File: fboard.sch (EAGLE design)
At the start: 41 parts, among them U1 ATMEGA328PB-AU, U2 MPU-6050

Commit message: fixed schematic
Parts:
- removed C8: 0.1uF, rcl:C-USC0805
- removed R12: 330R, rcl:R-US_R0805
- removed R13: 2.7kR, rcl:R-US_R0805
- removed R14, R15: 4.7kR, rcl:R-US_R0805
- removed U$1: SS14, SS14:SS14
- removed U$2: SK-3296S-01-L1, CustomParts:SK-3296S-01-L1
- removed U$3: RK-2032, CustomParts:RK-2032
- added BAT1: RK-2032, CustomParts:RK-2032
- added D1: MBR0520LT, diode:MBR0520LT
- added Q1: SL2305, SL2305:SL2305
- added S1: SK-3296S-01-L1, CustomParts:SK-3296S-01-L1
- added U3: SN74HC138PW, SN74HC138PW:SN74HC138PW
- C1, C2, C3, C4: device rcl:C-USC0805 -> rcl:C-EUC0805
- C5: value 0.1uF -> 10nF; device rcl:C-USC0805 -> rcl:C-EUC0805
- C6: value 10nF -> 2nF; device rcl:C-USC0805 -> rcl:C-EUC0805
- C7: value 2nF -> 0.1uF; device rcl:C-USC0805 -> rcl:C-EUC0805
- R1, R2, R3, R4, R5, R6, R7, R8, R9: device rcl:R-US_R0805 -> rcl:R-EU_R0805
- R10, R11: value 330R -> 4.7kR; device rcl:R-US_R0805 -> rcl:R-EU_R0805
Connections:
- removed net B3: ISP1.MOSI, R10.1
- removed net B4: ISP1.MISO, R11.2
- removed net B5: ISP1.SCK, R12.2
- removed net N$10: LED4.A, R4.2
- removed net N$11: LED9.A, R5.2
- removed net N$12: LED5.A, R6.2
- removed net N$13: LED6.A, R7.2
- removed net N$14: LED7.A, R8.2
- removed net N$15: LED8.A, R9.2
- removed net N$16: U$1.C, U$2.3
- removed net N$2: LED1.A, R1.2
- removed net PB0: R6.1, U1.PB0(ICP1/CLKO/PTCXY)
- removed net PB1: R5.1, U1.PB1(OC1A/PTCXY)
- removed net PB2: R4.1, U1.PB2(!SS0!/OC1B/PTCXY)
- removed net VOLTAGEPROTEC: U$1.A, U$3.+
- new net 3V_INPUT: BAT1.+, D1.A, ISP1.VCC, Q1.D
- new net N$1: LED2.A, R2.1
- new net N$19: LED1.C, R1.2
- new net N$3: LED3.A, R3.1
- new net N$4: LED4.A, R4.1
- new net N$5: LED9.A, R9.1
- new net N$6: LED5.A, R5.1
- new net N$7: LED6.A, R6.1
- new net PB6: LED1.A, U1.PB6(XTAL1/TOSC1)
- new net PB7: U1.PB7(XTAL2/TOSC2), U3.G1
- new net VPROTEC: D1.C, Q1.S, S1.1
- new net Y0: LED8.C, U3.Y0
- new net Y1: LED7.C, U3.Y1
- new net Y2: LED6.C, U3.Y2
- new net Y3: LED5.C, U3.Y3
- new net Y4: LED9.C, U3.Y4
- new net Y5: LED4.C, U3.Y5
- new net Y6: LED3.C, U3.Y6
- new net Y7: LED2.C, U3.Y7
- net CPOUT: now also C6.1; no longer C7.1
- net GND: now also BAT1.-, C3.2, C4.2, C6.2, C7.1, Q1.G, R1.1, S1.3, U3.GND; no longer C3.1, C4.1, C6.1, C7.2, C8.1, LED1.C, LED2.C, LED3.C, LED4.C, LED5.C, LED6.C, LED7.C, LED8.C, LED9.C, U$3.-
- net N$8: now also LED7.A, R7.1; no longer LED2.A, R2.2
- net N$9: now also LED8.A, R8.1; no longer LED3.A, R3.2
- net PB3: now also ISP1.MOSI; no longer R10.2, R3.1
- net PB4: now also ISP1.MISO; no longer R11.1, R2.1
- net PB5: now also ISP1.SCK; no longer R1.1, R12.1
- net PC4: now also R11.1; no longer R15.2
- net PC5: now also R10.1; no longer R14.2
- net PC6: no longer R13.2
- net PD5: now also U3.C; no longer R9.1
- net PD6: now also U3.B; no longer R8.1
- net PD7: now also U3.A; no longer R7.1
- net REGOUT: now also C4.1; no longer C5.1
- net VCC: now also C3.1, C5.1, C7.2, R10.2, R11.2, R2.2, R3.2, R4.2, R5.2, R6.2, R7.2, R8.2, R9.2, S1.2, U3.VCC; no longer C3.2, C4.2, C6.2, C8.2, ISP1.VCC, R13.1, R14.1, R15.1, U$2.1
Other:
- note added: "11/8/2020"
- note added: "2"
- note removed: "1"
- note removed: "11/5/2020"
- moved on the sheet: C1, C2, C3, C4, C5, C6, C7, ISP1, LED1, LED2, LED3, LED4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

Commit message: fixed more stuff
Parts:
- BAT1: device CustomParts:RK-2032 -> ECE_388_CustomParts_V1.1:RK-2032
- D1: value MBR0520LT -> SCHOTTKY_SS14L; device diode:MBR0520LT -> ECE_388_CustomParts_V1.1:SCHOTTKY_SS14L
- S1: device CustomParts:SK-3296S-01-L1 -> ECE_388_CustomParts_V1.1:SK-3296S-01-L1
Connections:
- net 3V_INPUT renamed BAT_3V
- net PB3 renamed MOSI
- net PB4 renamed MISO
- net PB5 renamed SCK
- net PB6 renamed PB6_LED1
- net PB7 renamed D_EN
- net PC4 renamed SDA0
- net PC5 renamed SCL0
- net PC6 renamed RST
- net PD5 renamed D_INPUT_C
- net PD6 renamed D_INPUT_B
- net PD7 renamed D_INPUT_A
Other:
- note added: "Fiducials"
- note added: "Power Input/Voltage Protection"
- note added: "uController"
- note added: "uController Inputs"
- note added: "uController Outputs"
- moved on the sheet: BAT1, C2, C3, C7, ISP1, LED1, LED2, LED3, LED4, LED5, LED6, LED7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

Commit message: updated stuff
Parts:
- removed D1: SCHOTTKY_SS14L, ECE_388_CustomParts_V1.1:SCHOTTKY_SS14L
- removed S1: SK-3296S-01-L1, ECE_388_CustomParts_V1.1:SK-3296S-01-L1
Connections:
- removed net BAT_3V: BAT1.+, D1.A, ISP1.VCC, Q1.D
- removed net VPROTEC: D1.C, Q1.S, S1.1
- new net +3V3: C1.1, C2.1, C3.1, C5.1, C7.2, Q1.S, R10.2, R11.2, R2.2, R3.2, R4.2, R5.2, R6.2, R7.2, R8.2, R9.2, U1.AREF, U1.AVCC, U1.VCC, U2.VDD, U2.VLOGIC, U3.VCC
- net GND: no longer S1.3
- net VCC: now also BAT1.+, ISP1.VCC, Q1.D; no longer C1.1, C2.1, C3.1, C5.1, C7.2, R10.2, R11.2, R2.2, R3.2, R4.2, R5.2, R6.2, R7.2, R8.2, R9.2, S1.2, U1.AREF, U1.AVCC, U1.VCC, U2.VDD, U2.VLOGIC, U3.VCC
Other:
- moved on the sheet: C1, C4, C5, C6, Q1, R10, R11, U2

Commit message: board stuff
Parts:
- removed R10, R11: 4.7kR, rcl:R-EU_R0805
- removed R5, R6, R7, R8, R9: 330R, rcl:R-EU_R0805
- R2, R3, R4: value 330R -> 4.7kR
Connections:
- net CPOUT renamed N$2
- net REGOUT renamed N$1
- removed net N$1 (its old number): LED2.A, R2.1
- removed net N$19: LED1.C, R1.2
- removed net N$3: LED3.A, R3.1
- removed net N$4: LED4.A, R4.1
- removed net N$5: LED9.A, R9.1
- removed net N$6: LED5.A, R5.1
- removed net N$7: LED6.A, R6.1
- removed net N$8: LED7.A, R7.1
- removed net N$9: LED8.A, R8.1
- removed net VCC: BAT1.+, ISP1.VCC, Q1.D
- new net LED_LINE: LED1.A, LED2.A, LED3.A, LED4.A, LED5.A, LED6.A, LED7.A, LED8.A, LED9.A, R1.1
- new net N$12: BAT1.+, Q1.D
- net +3V3: now also C7.1, ISP1.VCC, R1.2; no longer C7.2, R10.2, R11.2, R5.2, R6.2, R7.2, R8.2, R9.2
- net GND: now also C7.2; no longer C7.1, R1.1
- net PB6_LED1: now also LED1.C; no longer LED1.A
- net RST: now also R4.1
- net SCL0: now also R2.1; no longer R10.1
- net SDA0: now also R3.1; no longer R11.1
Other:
- note added: "11/10/2020"
- note added: "3"
- note removed: "11/8/2020"
- note removed: "2"
- moved on the sheet: C2, C3, C4, C6, C7, LED1, R1, R2, R3, R4

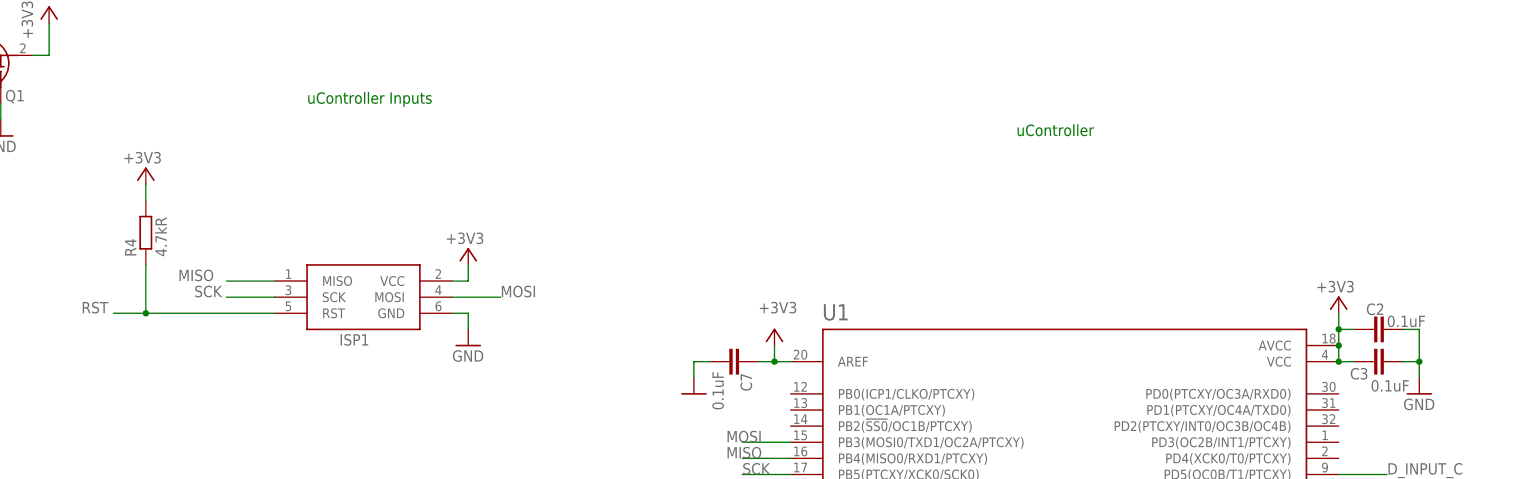
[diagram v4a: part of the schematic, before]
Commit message: moved a capacitor to reduce noise for pullups
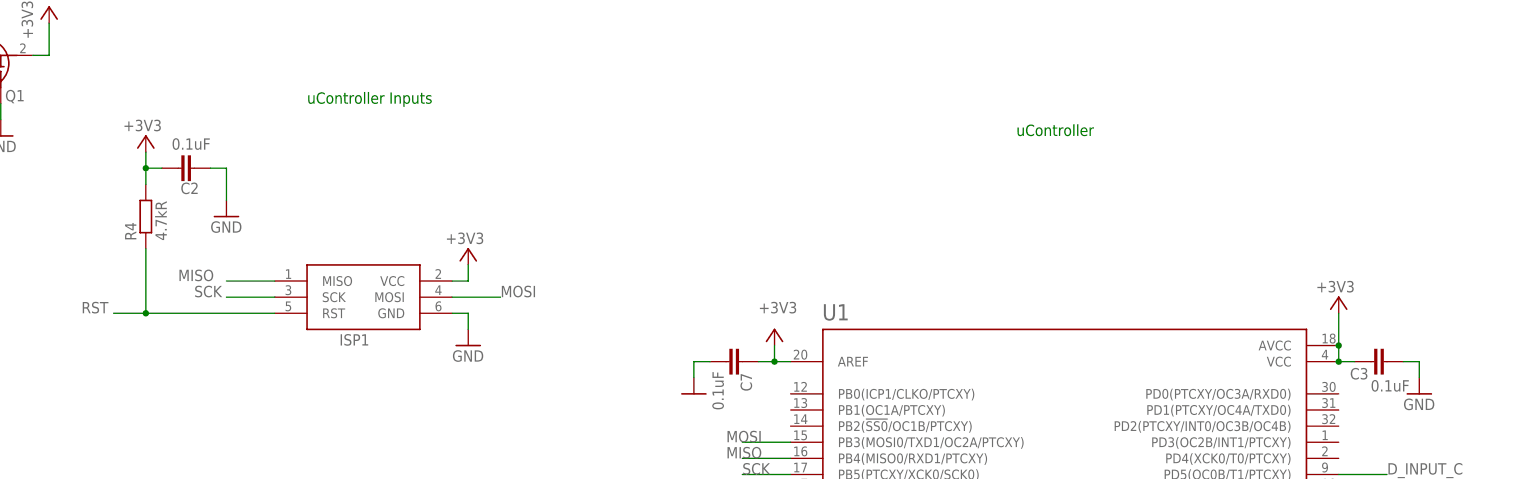
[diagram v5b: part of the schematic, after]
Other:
- moved on the sheet: C2, R4
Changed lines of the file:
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@@
 <part name="LED7" library="adafruit" library_urn="urn:adsk.eagle:library:420" deviceset="LED" device="CHIP-LED0805" package3d_urn="urn:adsk.eagle:package:6240557/1"/>
 <part name="LED8" library="adafruit" library_urn="urn:adsk.eagle:library:420" deviceset="LED" device="CHIP-LED0805" package3d_urn="urn:adsk.eagle:package:6240557/1"/>
-<part name="C2" library="rcl" library_urn="urn:adsk.eagle:library:334" deviceset="C-EU" device="C0805" package3d_urn="urn:adsk.eagle:package:23617/2" value="0.1uF"/>
 <part name="C3" library="rcl" library_urn="urn:adsk.eagle:library:334" deviceset="C-EU" device="C0805" package3d_urn="urn:adsk.eagle:package:23617/2" value="0.1uF"/>
 <part name="LED1" library="adafruit" library_urn="urn:adsk.eagle:library:420" deviceset="LED" device="CHIP-LED0805" package3d_urn="urn:adsk.eagle:package:6240557/1"/>
@@
 <part name="R3" library="rcl" library_urn="urn:adsk.eagle:library:334" deviceset="R-EU_" device="R0805" package3d_urn="urn:adsk.eagle:package:23553/2" value="4.7kR"/>
 <part name="R4" library="rcl" library_urn="urn:adsk.eagle:library:334" deviceset="R-EU_" device="R0805" package3d_urn="urn:adsk.eagle:package:23553/2" value="4.7kR"/>
+<part name="C2" library="rcl" library_urn="urn:adsk.eagle:library:334" deviceset="C-EU" device="C0805" package3d_urn="urn:adsk.eagle:package:23617/2" value="0.1uF"/>
+<part name="GND4" library="supply1" library_urn="urn:adsk.eagle:library:371" deviceset="GND" device=""/>
 </parts>
 <sheets>
@@
 <attribute name="VALUE" x="115.824" y="117.221" size="1.778" layer="96"/>
 </instance>
-<instance part="+3V12" gate="G$1" x="55.88" y="213.36" smashed="yes">
-<attribute name="VALUE" x="58.42" y="215.9" size="1.778" layer="96" rot="R180"/>
+<instance part="+3V12" gate="G$1" x="55.88" y="218.44" smashed="yes">
+<attribute name="VALUE" x="58.42" y="220.98" size="1.778" layer="96" rot="R180"/>
 </instance>
 <instance part="+3V8" gate="G$1" x="243.84" y="193.04" smashed="yes">
@@
 <attribute name="VALUE" x="351.028" y="150.495" size="1.778" layer="96" rot="MR180"/>
 </instance>
-<instance part="C2" gate="G$1" x="248.92" y="187.96" smashed="yes" rot="R90">
-<attribute name="NAME" x="251.079" y="192.024" size="1.778" layer="95" rot="R180"/>
-<attribute name="VALUE" x="257.556" y="190.119" size="1.778" layer="96" rot="R180"/>
-</instance>
 <instance part="C3" gate="G$1" x="248.92" y="182.88" smashed="yes" rot="R90">
 <attribute name="NAME" x="248.539" y="181.864" size="1.778" layer="95" rot="R180"/>
@@
 <attribute name="VALUE" x="64.262" y="118.11" size="1.778" layer="96" rot="R90"/>
 </instance>
-<instance part="R4" gate="G$1" x="55.88" y="203.2" smashed="yes" rot="R90">
-<attribute name="NAME" x="54.3814" y="199.39" size="1.778" layer="95" rot="R90"/>
-<attribute name="VALUE" x="59.182" y="199.39" size="1.778" layer="96" rot="R90"/>
+<instance part="R4" gate="G$1" x="55.88" y="205.74" smashed="yes" rot="R90">
+<attribute name="NAME" x="54.3814" y="201.93" size="1.778" layer="95" rot="R90"/>
+<attribute name="VALUE" x="59.182" y="201.93" size="1.778" layer="96" rot="R90"/>
+</instance>
+<instance part="C2" gate="G$1" x="60.96" y="213.36" smashed="yes" rot="R90">
+<attribute name="NAME" x="61.341" y="209.296" size="1.778" layer="95"/>
+<attribute name="VALUE" x="59.944" y="216.281" size="1.778" layer="96"/>
+</instance>
+<instance part="GND4" gate="1" x="68.58" y="205.74" smashed="yes">
+<attribute name="VALUE" x="66.04" y="203.2" size="1.778" layer="96"/>
 </instance>
 </instances>
@@
 <pinref part="ISP1" gate="G$1" pin="RST"/>
 <wire x1="55.88" y1="190.5" x2="50.8" y2="190.5" width="0.1524" layer="91"/>
-<wire x1="55.88" y1="198.12" x2="55.88" y2="190.5" width="0.1524" layer="91"/>
 <junction x="55.88" y="190.5"/>
 <pinref part="R4" gate="G$1" pin="1"/>
+<wire x1="55.88" y1="200.66" x2="55.88" y2="190.5" width="0.1524" layer="91"/>
 </segment>
 </net>
@@
 </segment>
 <segment>
-<wire x1="254" y1="187.96" x2="256.54" y2="187.96" width="0.1524" layer="91"/>
-<wire x1="256.54" y1="187.96" x2="256.54" y2="182.88" width="0.1524" layer="91"/>
 <wire x1="256.54" y1="182.88" x2="254" y2="182.88" width="0.1524" layer="91"/>
 <pinref part="GND2" gate="1" pin="GND"/>
 <wire x1="256.54" y1="180.34" x2="256.54" y2="182.88" width="0.1524" layer="91"/>
-<junction x="256.54" y="182.88"/>
+<pinref part="C3" gate="G$1" pin="2"/>
+</segment>
+<segment>
 <pinref part="C2" gate="G$1" pin="2"/>
-<pinref part="C3" gate="G$1" pin="2"/>
+<wire x1="66.04" y1="213.36" x2="68.58" y2="213.36" width="0.1524" layer="91"/>
+<pinref part="GND4" gate="1" pin="GND"/>
+<wire x1="68.58" y1="213.36" x2="68.58" y2="208.28" width="0.1524" layer="91"/>
 </segment>
 </net>
@@
 </segment>
 <segment>
-<wire x1="55.88" y1="208.28" x2="55.88" y2="210.82" width="0.1524" layer="91"/>
+<wire x1="55.88" y1="210.82" x2="55.88" y2="213.36" width="0.1524" layer="91"/>
 <pinref part="+3V12" gate="G$1" pin="+3V3"/>
 <pinref part="R4" gate="G$1" pin="2"/>
+<pinref part="C2" gate="G$1" pin="1"/>
+<wire x1="55.88" y1="213.36" x2="55.88" y2="215.9" width="0.1524" layer="91"/>
+<wire x1="58.42" y1="213.36" x2="55.88" y2="213.36" width="0.1524" layer="91"/>
+<junction x="55.88" y="213.36"/>
 </segment>
 <segment>
 <wire x1="243.84" y1="182.88" x2="243.84" y2="185.42" width="0.1524" layer="91"/>
-<wire x1="243.84" y1="185.42" x2="243.84" y2="187.96" width="0.1524" layer="91"/>
-<wire x1="243.84" y1="187.96" x2="246.38" y2="187.96" width="0.1524" layer="91"/>
 <pinref part="+3V8" gate="G$1" pin="+3V3"/>
-<wire x1="243.84" y1="187.96" x2="243.84" y2="190.5" width="0.1524" layer="91"/>
-<junction x="243.84" y="187.96"/>
+<wire x1="243.84" y1="185.42" x2="243.84" y2="190.5" width="0.1524" layer="91"/>
 <pinref part="U1" gate="G$1" pin="VCC"/>
 <pinref part="U1" gate="G$1" pin="AVCC"/>
@@
 <wire x1="243.84" y1="182.88" x2="246.38" y2="182.88" width="0.1524" layer="91"/>
 <junction x="243.84" y="182.88"/>
-<pinref part="C2" gate="G$1" pin="1"/>
 <pinref part="C3" gate="G$1" pin="1"/>
 </segment>

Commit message: board stuff
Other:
- note added: "11/11/2020"
- note added: "4"
- note removed: "11/10/2020"
- note removed: "3"
- moved on the sheet: C2, C5, C6, R4

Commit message: grounded ~g2a and ~g2b
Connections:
- net GND: now also U3.!G2A, U3.!G2B
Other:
- note added: "11/17/2020"
- note added: "5"
- note removed: "11/11/2020"
- note removed: "4"
- note removed: "uController Outputs"
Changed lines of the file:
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@@
 <part name="C4" library="rcl" library_urn="urn:adsk.eagle:library:334" deviceset="C-EU" device="C0805" package3d_urn="urn:adsk.eagle:package:23617/2" value="0.1uF"/>
 <part name="C1" library="rcl" library_urn="urn:adsk.eagle:library:334" deviceset="C-EU" device="C0805" package3d_urn="urn:adsk.eagle:package:23617/2" value="0.1uF"/>
+<part name="GND7" library="supply1" library_urn="urn:adsk.eagle:library:371" deviceset="GND" device=""/>
 </parts>
 <sheets>
 <sheet>
 <plain>
-<text x="358.14" y="10.16" size="1.778" layer="91">11/11/2020</text>
+<text x="358.14" y="10.16" size="1.778" layer="91">11/17/2020</text>
 <text x="358.14" y="15.24" size="1.778" layer="91">Michael Bourgeois</text>
 <text x="342.9" y="20.32" size="1.778" layer="91">Title:</text>
@@
 <text x="342.9" y="10.16" size="1.778" layer="91">Date:</text>
 <text x="375.92" y="5.08" size="1.778" layer="91">Rev.</text>
-<text x="381" y="5.08" size="1.778" layer="91">4</text>
+<text x="381" y="5.08" size="1.778" layer="91">5</text>
 <text x="15.24" y="248.92" size="1.778" layer="91">Power Input/Voltage Protection</text>
 <text x="81.28" y="223.52" size="1.778" layer="91">uController Inputs</text>
 <text x="193.04" y="218.44" size="1.778" layer="91">uController</text>
-<text x="322.58" y="182.88" size="1.778" layer="91">uController Outputs</text>
 <text x="259.08" y="27.94" size="1.778" layer="91">Fiducials</text>
 </plain>
@@
 <attribute name="NAME" x="116.459" y="146.304" size="1.778" layer="95" rot="R180"/>
 <attribute name="VALUE" x="122.936" y="141.859" size="1.778" layer="96" rot="R180"/>
+</instance>
+<instance part="GND7" gate="1" x="297.18" y="109.22" smashed="yes">
+<attribute name="VALUE" x="294.64" y="106.68" size="1.778" layer="96"/>
 </instance>
 </instances>
@@
 <wire x1="76.2" y1="213.36" x2="76.2" y2="208.28" width="0.1524" layer="91"/>
 </segment>
-</net>
+<segment>
+<pinref part="U3" gate="A" pin="!G2B"/>
+<pinref part="GND7" gate="1" pin="GND"/>
+<wire x1="299.72" y1="124.46" x2="297.18" y2="124.46" width="0.1524" layer="91"/>
+<wire x1="297.18" y1="124.46" x2="297.18" y2="111.76" width="0.1524" layer="91"/>
+<pinref part="U3" gate="A" pin="!G2A"/>
+<wire x1="299.72" y1="127" x2="297.18" y2="127" width="0.1524" layer="91"/>
+<wire x1="297.18" y1="127" x2="297.18" y2="124.46" width="0.1524" layer="91"/>
+<junction x="297.18" y="124.46"/>
+</segment>
+</net>
